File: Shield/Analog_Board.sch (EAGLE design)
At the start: 62 parts, among them IC1 INA105U, IC2 ACPL-C87A-000E, IC3 ACPL-C87A-000E, IC4 INA105U, IC5 ACPL-C87A-000E, IC6 INA105U, IC7 ACPL-C87A-000E, IC8 INA105U

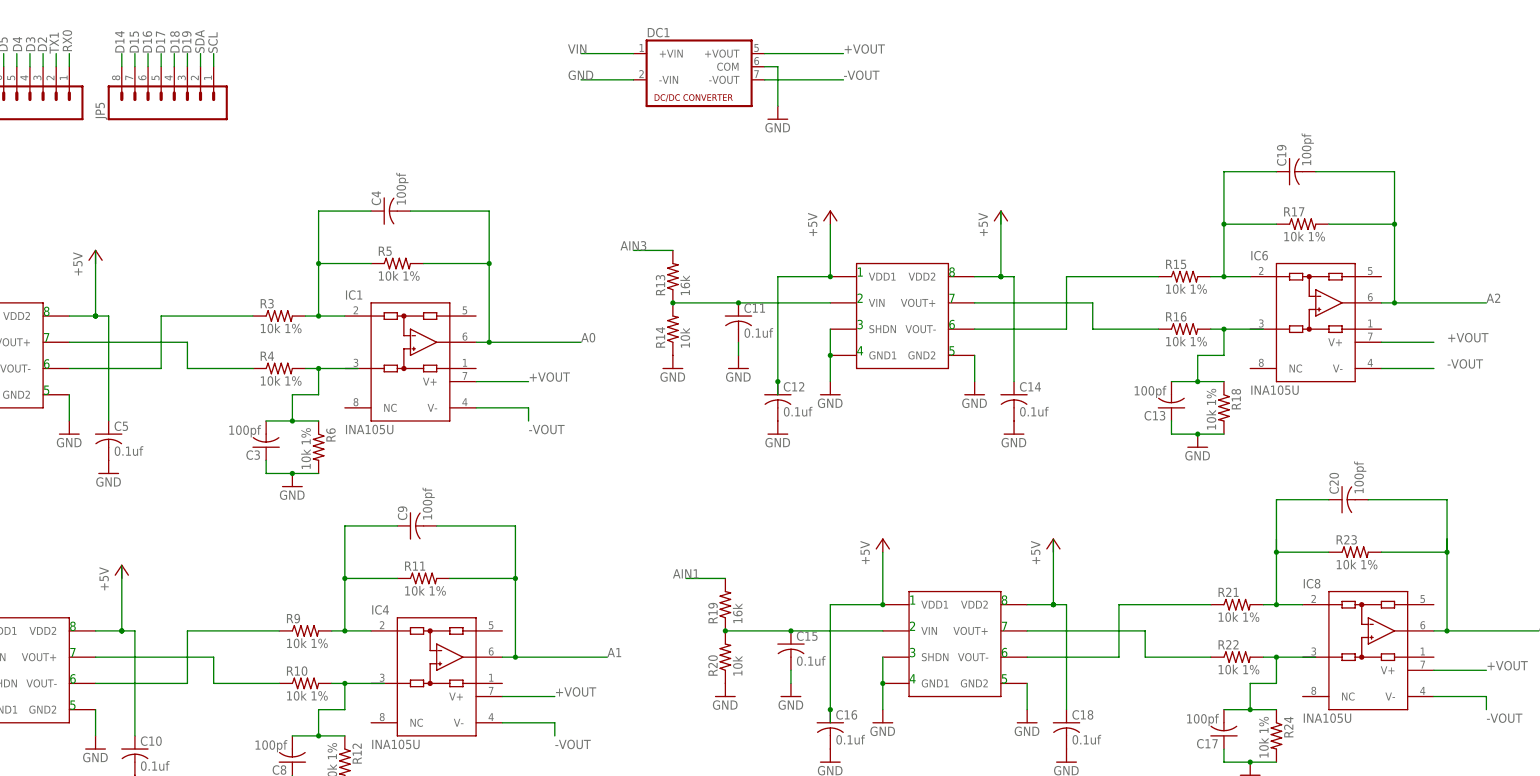
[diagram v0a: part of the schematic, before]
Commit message: Newer version of analog board, new version of DueD
Dued board now properly sized for the new case.
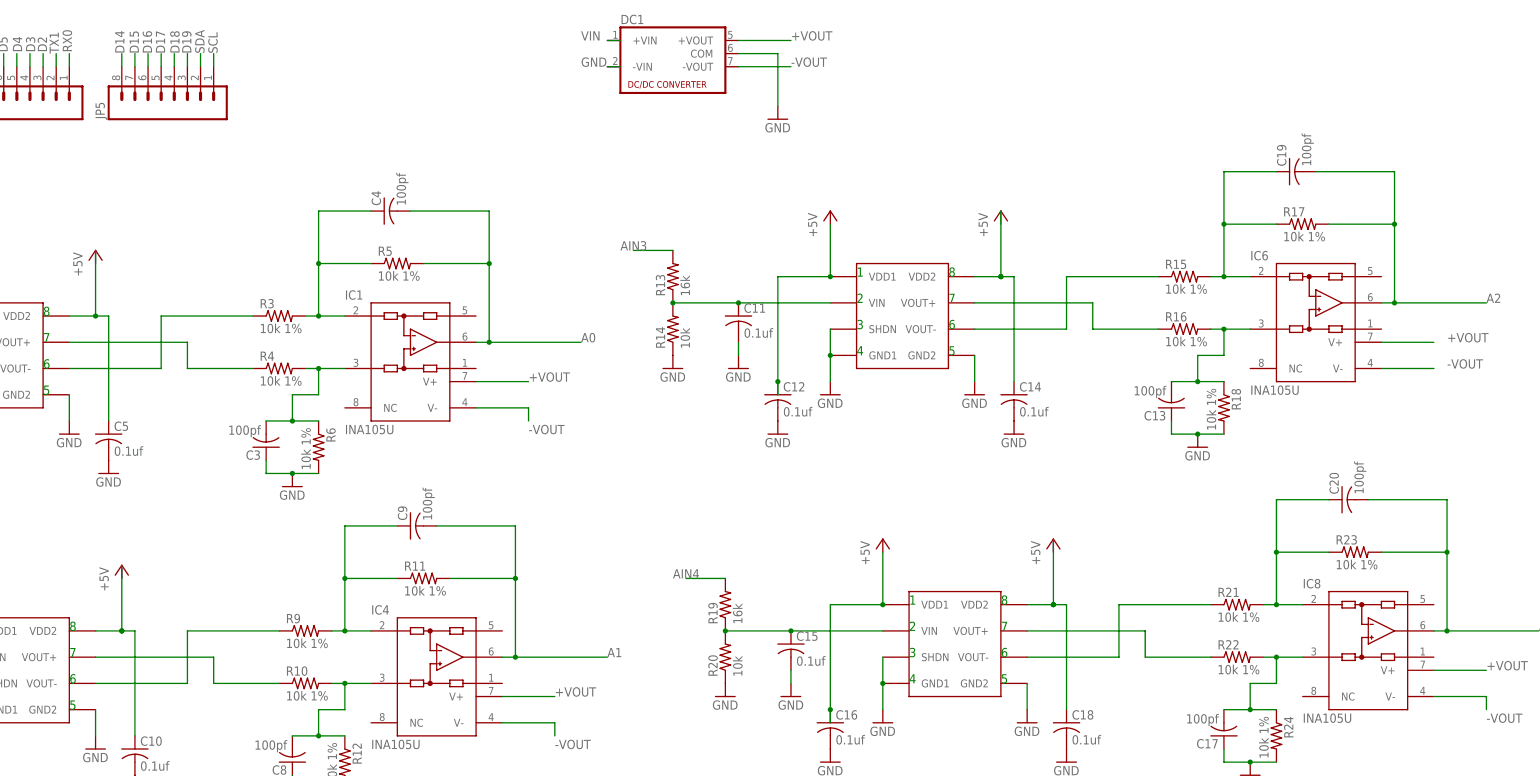
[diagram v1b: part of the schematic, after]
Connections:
- net -VOUT: now also DC1.-VOUT
- net AIN1: no longer R19.2
- net AIN4: now also R19.2
- net N$14: now also IC4.+IN
- net N$22: now also IC6.+IN
- net N$30: now also IC8.+IN
- net N$9: now also IC1.+IN
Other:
- moved on the sheet: DC1
